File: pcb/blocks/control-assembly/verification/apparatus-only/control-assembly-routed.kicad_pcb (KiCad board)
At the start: 6 copper layers, 164 x 234 mm, 19 parts, among them SW1 ?, SW2 ?, U1 ?, U2 ?

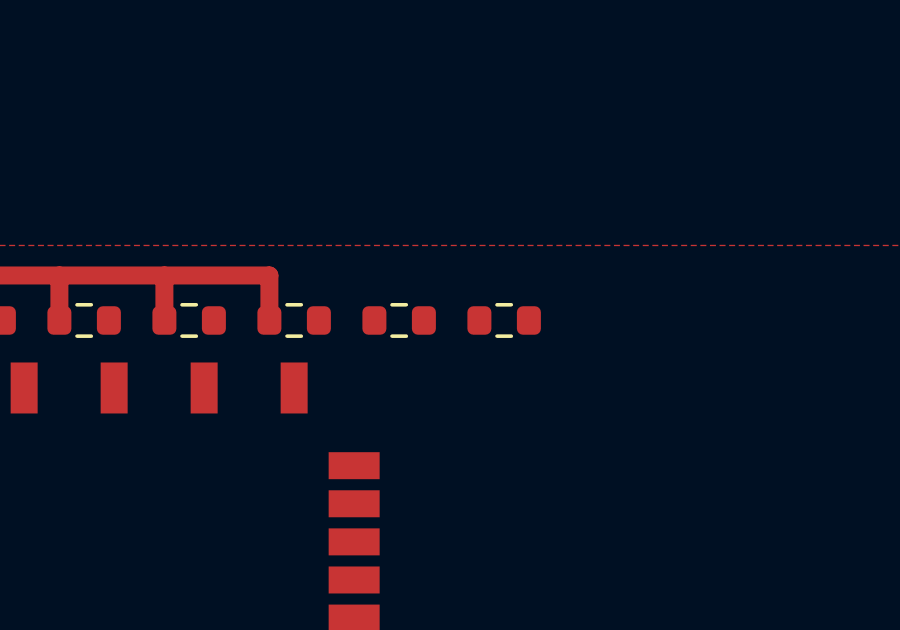
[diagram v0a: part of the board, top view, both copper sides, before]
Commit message: fix(control-assembly): flat schematic parity, prototype vendor fallback, overlay net re-assert
- compose_assembly: use the flat strict-candidate schematic layout and pass
  BOM values into generate_candidate_board, moving schematic parity 98 -> 0
  (19 footprint_symbol_mismatch + 79 net_conflict). Regenerate the combined
  bridge/source map so SW1/SW2 are the real SW_SPST_EVQP7A.
- block_source: fall back to the buck prototype library for footprints absent
  from KiCad stock and pcb/libs, recording prototype-lib provenance; drop
  compose_assembly._stock_root_with_overrides. Persist
  assembly-candidate/library-provenance.json.
- run_block.build_assembly_task_contract: derive the pad census from pad
  identities, not physical pad count (a real switch repeats 1,1,2,2); mirrors
  the accepted MCU-profile fix.
- run_control_assembly: re-assert production track net identity by name after
  the KiCad refill so net_reassigned is 0; measure ground continuity across
  the section/production boundary. The section-pour clip was implemented and
  measured to raise introduced findings and break the cross-view endpoints, so
  it is recorded as rejected (enabled false), not silently omitted.
- compose_blocks: compare zone identity (net/layer/filled), not polygon
  subdivision, in the cross-view comparison.
- tests + docs updated for the above.
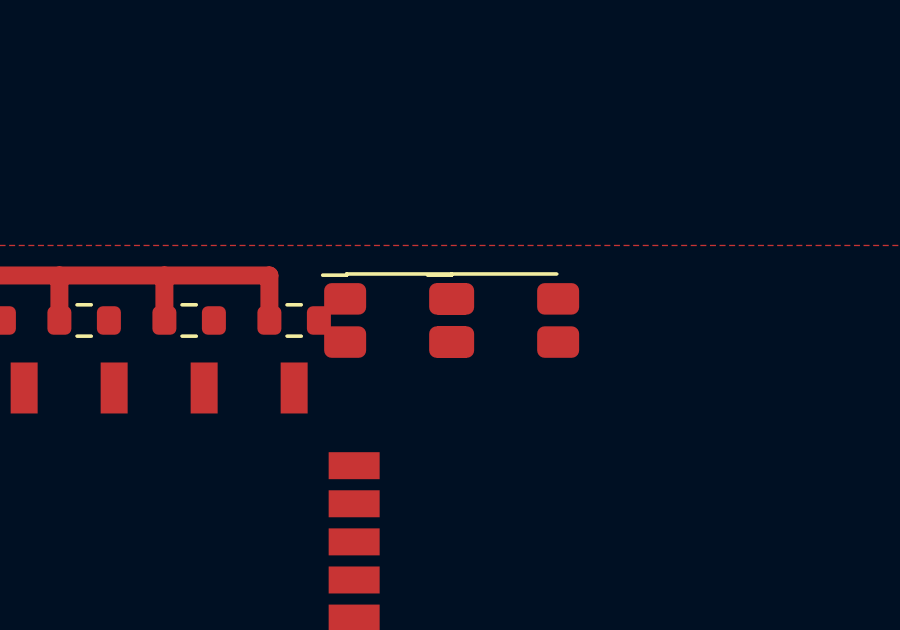
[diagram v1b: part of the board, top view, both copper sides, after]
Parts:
- C1: value ? -> CL32B106KBJZW6E
- C2, C5, C6: value ? -> C0603C104K5RACTU
- C3, C4: value ? -> CL32B226KAJNNWE
- C7: value ? -> GRM21BR71A106KE51L
- C8: value ? -> GRM188R71A105KA61D
- L1: value ? -> SRP1265A-5R6M
- R1: value ? -> RC0603FR-07100KL
- R2: value ? -> RC0603FR-0722K1L
- R3, R4: value ? -> RC0603FR-0710KL
- R5, R6: value ? -> RC0603FR-074K7L
- SW1, SW2: value ? -> EVQ-P7A01P; footprint Resistor_SMD:R_0603_1608Metric -> Button_Switch_SMD:SW_SPST_EVQP7A
- U1: value ? -> LMR51430XDDCR
- U2: value ? -> ESP32-S3-WROOM-1-N8R8
